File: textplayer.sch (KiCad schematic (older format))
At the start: 42 parts

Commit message: first pcb attempts
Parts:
- removed U?: STM32F411xC/xE, symbol STM32F411xC/xE
- added R14, R17: 0, Resistors_SMD:R_0805_HandSoldering, symbol R
- added R15, R16: DNP, Resistors_SMD:R_0805_HandSoldering, symbol R
- added U6: STM32F411xC/xE, symbol STM32F411xC/xE
- BT1: renamed from BT?; footprint (none) -> Morn_Mechanical:BCAAPC
- C1, C10, C11, C2, C3, C4, C5, C6, C7, C9: renamed from C?; footprint (none) -> Capacitors_SMD:C_0805_HandSoldering
- C8: renamed from C?; footprint (none) -> Capacitors_Tantalum_SMD:CP_Tantalum_Case-B_EIA-3528-21_Hand
- J1: renamed from J?; footprint (none) -> Pin_Headers:Pin_Header_Straight_2x03_Pitch2.54mm
- J2, J4: renamed from J?; footprint (none) -> Pin_Headers:Pin_Header_Straight_2x10_Pitch2.54mm
- J3: renamed from J?; footprint (none) -> Pin_Headers:Pin_Header_Straight_1x06_Pitch2.54mm
- L1: renamed from L?; footprint (none) -> Morn_SMD:Inductor_B82462G4
- R1, R10, R11, R12, R13, R2, R3, R4, R5, R6, R7, R8, R9: renamed from R?; footprint (none) -> Resistors_SMD:R_0805_HandSoldering
- SW1, SW2, SW3, SW4, SW5, SW6: renamed from SW?; footprint (none) -> Buttons_Switches_SMD:SW_SPST_B3S-1000
- U1: renamed from U?; footprint (none) -> Housings_SSOP:TSSOP-56_6.1x14mm_Pitch0.5mm
- U2: renamed from U?; footprint (none) -> Morn_ThroughHole:VIM-878
- U3: renamed from U?; footprint (none) -> Housings_SSOP:TSSOP-8_4.4x3mm_Pitch0.65mm
- U4: renamed from U?; footprint QFN/MLF32 -> Housings_DFN_QFN:QFN-32-1EP_5x5mm_Pitch0.5mm
- U5: renamed from U?; value TPS61020 -> TPS61020DRC; footprint (none) -> Morn_SMD_NoLeads:S-PVSON-N10
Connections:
- net +3V3: now also U6.1 (VBAT), U6.24 (VDD), U6.36 (VDD), U6.48 (VDD), U6.9 (VDDA_VREF+)
- net BOOT0: now also U6.44 (BOOT0)
- net DTR: now also U6.10 (PA0)
- net E1: now also U6.43 (PB7)
- net E10: now also U6.25 (PB12)
- net E11: now also U6.19 (PB1)
- net E12: now also U6.20 (PB2)
- net E13: now also U6.21 (PB10)
- net E14: now also U6.2 (PC13)
- net E15: now also U6.3 (PC14-OSC32_IN)
- net E16: now also U6.4 (PC15-OSC32_OUT)
- net E17: now also U6.5 (PH0-OSC_IN)
- net E18: now also U6.6 (PH0-OSC_OUT)
- net E2: now also U6.42 (PB6)
- net E3: now also U6.41 (PB5)
- net E4: now also U6.33 (PA12)
- net E5: now also U6.32 (PA11)
- net E6: now also U6.29 (PA8)
- net E7: now also U6.28 (PB15)
- net E8: now also U6.27 (PB14)
- net E9: now also U6.26 (PB13)
- net GND: now also U6.23 (VSS), U6.35 (VSS), U6.47 (VSS), U6.8 (VSSA_VREF-)
- net RESET: now also U6.7 (NRST)
- net RXD: now also R1.1, U4.26 ((ADC0/DI/SDA/PCINT0)PA0), R16.2, R17.2, U6.31 (PA10); no longer J3.5 (P5), U4.25 ((ADC1/DO/PCINT1)PA1)
- net SCL: now also U6.45 (PB8)
- net SDA: now also U6.46 (PB9)
- net SW_A: now also U6.17 (PA7)
- net SW_B: now also U6.18 (PB0)
- net SW_DN: now also U6.14 (PA4)
- net SW_LF: now also U6.15 (PA5)
- net SW_RI: now also U6.16 (PA6)
- net SW_UP: now also U6.13 (PA3)
- net TCK: now also U6.37 (PA14)
- net TDI: now also U6.38 (PA15)
- net TDO: now also U6.39 (PB3)
- net TMS: now also U6.34 (PA13)
- net TXD: now also U4.25 ((ADC1/DO/PCINT1)PA1), R14.2, R15.2, U6.30 (PA9); no longer J3.4 (P4), R1.1, U4.26 ((ADC0/DI/SDA/PCINT0)PA0)
- net VCAP_1: now also U6.22 (VCAP_1)
- net nTRST: now also U6.40 (PB4)
- new net: J3.4 (P4), R14.1, R16.1
- new net: J3.5 (P5), R15.1, R17.1

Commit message: placing...
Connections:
- net RESET: no longer J1.5 (P5), U4.11 ((ADC10/~RESET~/PCINT15)PB7)
- new net AVR_RESET: J1.5 (P5), U4.11 ((ADC10/~RESET~/PCINT15)PB7)
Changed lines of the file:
@@
 SCK
 Text Label 1700 950  2    60   ~ 0
-RESET
+AVR_RESET
 Text Label 2400 850  0    60   ~ 0
 MOSI
@@
 $EndComp
 Text Label 3250 2900 0    60   ~ 0
-RESET
+AVR_RESET
 Text Label 3250 2300 0    60   ~ 0
 MISO

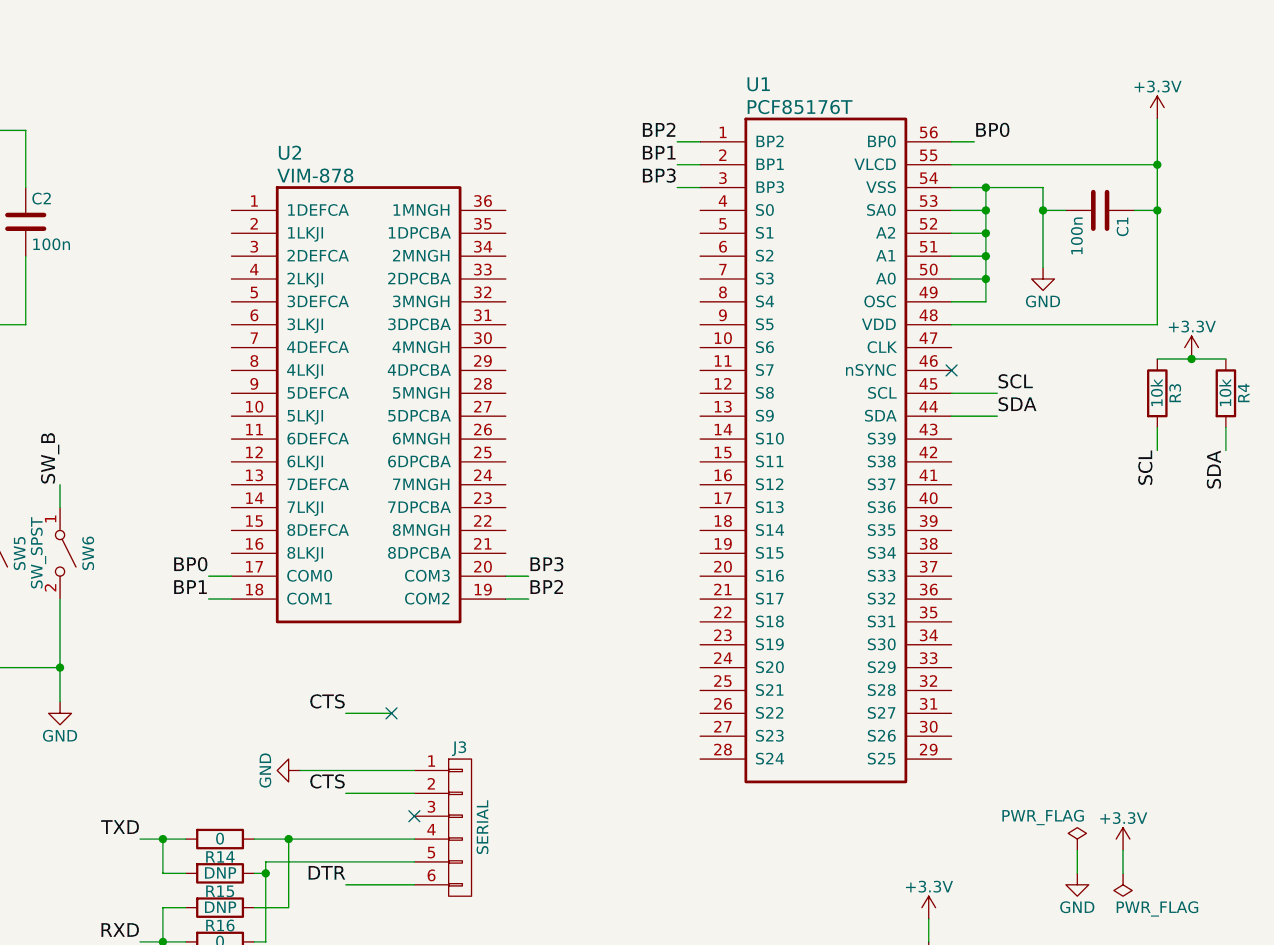
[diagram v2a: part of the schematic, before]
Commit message: displays schematic ausgelagert
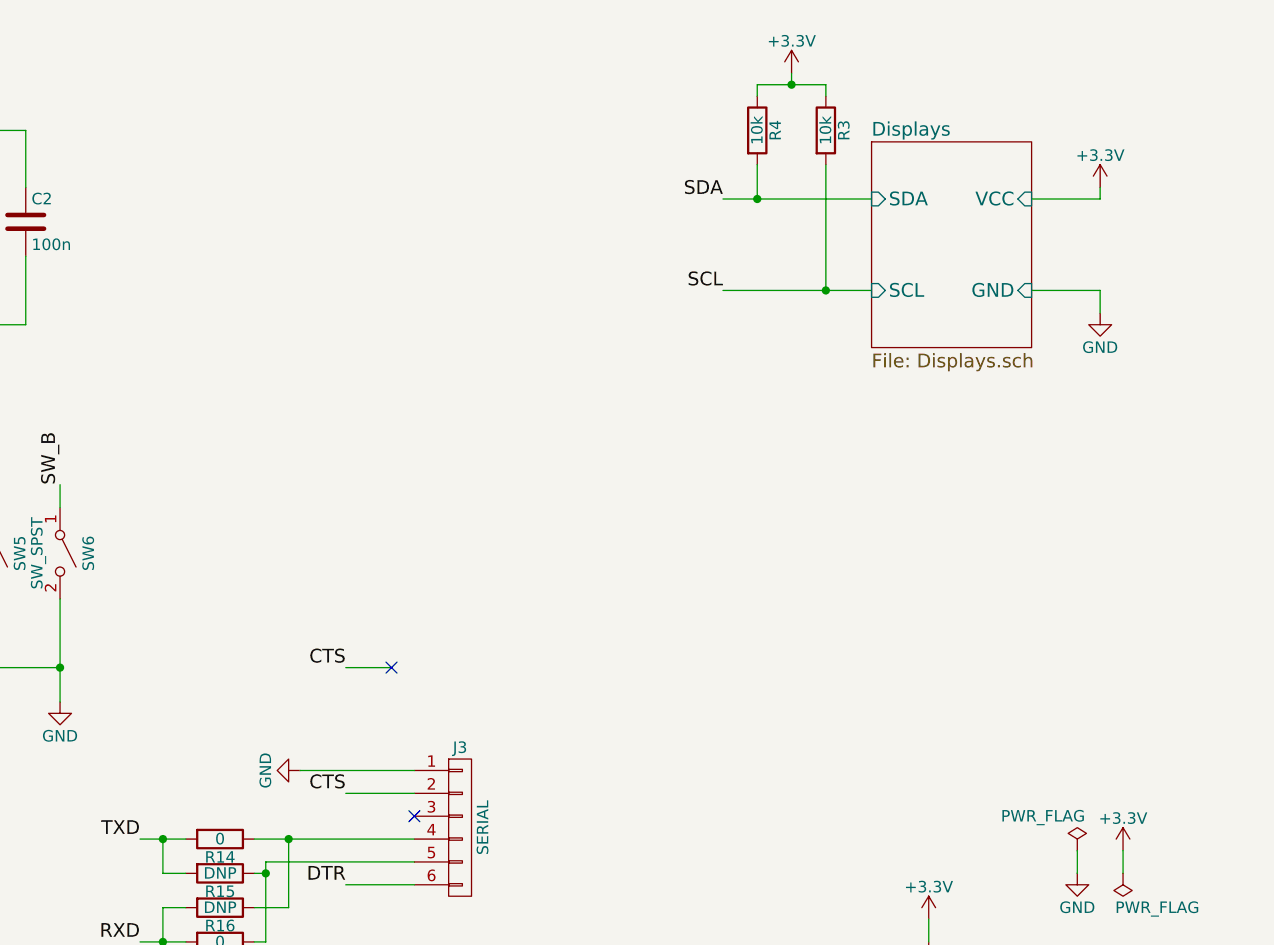
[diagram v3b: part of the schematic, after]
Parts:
- removed C1: 100n, Capacitors_SMD:C_0805_HandSoldering, symbol C
- removed U1: PCF85176T, Housings_SSOP:TSSOP-56_6.1x14mm_Pitch0.5mm, symbol PCF85176T
- removed U2: VIM-878, Morn_ThroughHole:VIM-878, symbol VIM-878
- U6: footprint (none) -> Housings_DFN_QFN:QFN-48-1EP_7x7mm_Pitch0.5mm
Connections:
- no-connect marks 9 -> 8
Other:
- moved on the sheet: R3, R4

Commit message: place should be done now
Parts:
- added J10: GND, Measurement_Points:Measurement_Point_Round-TH_Small, symbol CONN_01X01
- added J11: GND, Measurement_Points:Measurement_Point_Round-SMD-Pad_Big, symbol CONN_01X01
- added J12: VCC, Measurement_Points:Measurement_Point_Round-TH_Small, symbol CONN_01X01
- added J13: VCC, Measurement_Points:Measurement_Point_Round-SMD-Pad_Big, symbol CONN_01X01
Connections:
- net +3V3: now also J12.1 (P1), J13.1 (P1)
- net GND: now also J10.1 (P1), J11.1 (P1)
- net SDA: now also R1.2

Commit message: almost done..
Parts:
- added D1: LED, LEDs:LED_0805, symbol LED
- added R54: R, Resistors_SMD:R_0805_HandSoldering, symbol R
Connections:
- net +3V3: now also R54.1
- net GND: now also D1.1 (K)
- new net: D1.2 (A), R54.2
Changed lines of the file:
@@
 	10050 3200 10050 3250
 Connection ~ 9750 3150
+$Comp
+L LED D1
+U 1 1 58EA8F92
+P 6950 2050
+F 0 "D1" H 6950 2150 50  0000 C CNN
+F 1 "LED" H 6950 1950 50  0000 C CNN
+F 2 "LEDs:LED_0805" H 6950 2050 50  0001 C CNN
+F 3 "" H 6950 2050 50  0001 C CNN
+	1    6950 2050
+	0    -1   -1   0
+$EndComp
+$Comp
+L R R54
+U 1 1 58EA9269
+P 6950 1650
+F 0 "R54" V 7030 1650 50  0000 C CNN
+F 1 "R" V 6950 1650 50  0000 C CNN
+F 2 "Resistors_SMD:R_0805_HandSoldering" V 6880 1650 50  0001 C CNN
+F 3 "" H 6950 1650 50  0001 C CNN
+	1    6950 1650
+	1    0    0    -1
+$EndComp
+Wire Wire Line
+	6950 1800 6950 1900
+$Comp
+L GND #PWR037
+U 1 1 58EA94B1
+P 6950 2350
+F 0 "#PWR037" H 6950 2100 50  0001 C CNN
+F 1 "GND" H 6950 2200 50  0000 C CNN
+F 2 "" H 6950 2350 50  0001 C CNN
+F 3 "" H 6950 2350 50  0001 C CNN
+	1    6950 2350
+	1    0    0    -1
+$EndComp
+$Comp
+L +3.3V #PWR038
+U 1 1 58EA9B71
+P 6950 1350
+F 0 "#PWR038" H 6950 1200 50  0001 C CNN
+F 1 "+3.3V" H 6950 1490 50  0000 C CNN
+F 2 "" H 6950 1350 50  0001 C CNN
+F 3 "" H 6950 1350 50  0001 C CNN
+	1    6950 1350
+	1    0    0    -1
+$EndComp
+Wire Wire Line
+	6950 1350 6950 1500
+Wire Wire Line
+	6950 2200 6950 2350
 $EndSCHEMATC
